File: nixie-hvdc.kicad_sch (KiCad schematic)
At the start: 13 parts, among them Q1 IRF740, U1 MAX1771xSA

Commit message: almost done
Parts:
- added D3: PTVS18VZ1USK, Diode_SMD:Nexperia_DSN1608-2_1.6x0.8mm, symbol Diode:PTVS18VZ1USK
- added F1: 2A, symbol Device:Fuse
- added FB1: FerriteBead, symbol Device:FerriteBead
- added J1: USB_C_Receptacle_PowerOnly_6P, Connector_USB:USB_C_Receptacle_HRO_TYPE-C-31-M-17, symbol Connector:USB_C_Receptacle_PowerOnly_6P
- added J2, J3: Screw_Terminal_01x02, TerminalBlock_Phoenix:TerminalBlock_Phoenix_MKDS-1,5-2-5.08_1x02_P5.08mm_Horizontal, symbol Connector:Screw_Terminal_01x02
- added J4: Conn_01x10_Socket, Connector_PinHeader_2.54mm:PinHeader_1x10_P2.54mm_Vertical, symbol Connector:Conn_01x10_Socket
- added NX1: IN-12A, nixies-us:nixies-us-IN-12-DSUB-NOHOLE, symbol nixies-us:IN-12A
- added Q10, Q11, Q2, Q3, Q4, Q5, Q6, Q7, Q8, Q9: MPSA42, Package_TO_SOT_THT:TO-92_Inline, symbol Transistor_BJT:MPSA42
- added R10, R11, R12, R13, R14, R15, R16, R6, R7, R8, R9: 10k, symbol Device:R_US
- added R4, R5: 5.1k, symbol Device:R_US
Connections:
- net 180V: now also J3.1 (Pin_1), R6.2
- net GND: now also D3.1 (K), J1.A12 (GND), J1.B12 (GND), J1.S1 (SHIELD), J2.1 (Pin_1), J3.2 (Pin_2), Q10.1 (E), Q11.1 (E), Q2.1 (E), Q3.1 (E), Q4.1 (E), Q5.1 (E), Q6.1 (E), Q7.1 (E), Q8.1 (E), Q9.1 (E), R4.2, R5.2
- net at L1.2, Q1.2 (D): now also D1.2 (A)
- net +3V3: no longer names the net of C2.1, C3.1, L1.1, U1.2 (V+)
- net +3V3: now also FB1.2; no longer D1.2 (A)
- new net: Q2.2 (B), R7.2
- new net: Q6.2 (B), R11.2
- new net: Q10.2 (B), R15.2
- new net: Q8.2 (B), R13.2
- new net: Q11.2 (B), R16.2
- new net: Q3.2 (B), R8.2
- new net: Q5.2 (B), R10.2
- new net: J1.B5 (CC2), R4.1
- new net: Q7.2 (B), R12.2
- new net: NX1.A, R6.1
- new net: J1.A5 (CC1), R5.1
- new net: Q9.2 (B), R14.2
- new net: D3.2 (A), F1.2, FB1.1
- new net: Q4.2 (B), R9.2
- new net +12V: F1.1, J2.2 (Pin_2)
- new net +5V: J1.A9 (VBUS), J1.B9 (VBUS)
- new net CTRL_DIGIT_0: J4.10 (Pin_10), R7.1
- new net CTRL_DIGIT_1: J4.1 (Pin_1), R8.1
- new net CTRL_DIGIT_2: J4.2 (Pin_2), R9.1
- new net CTRL_DIGIT_3: J4.3 (Pin_3), R13.1
- new net CTRL_DIGIT_4: J4.4 (Pin_4), R14.1
- new net CTRL_DIGIT_5: J4.5 (Pin_5), R15.1
- new net CTRL_DIGIT_6: J4.6 (Pin_6), R10.1
- new net CTRL_DIGIT_7: J4.7 (Pin_7), R11.1
- new net CTRL_DIGIT_8: J4.8 (Pin_8), R12.1
- new net CTRL_DIGIT_9: J4.9 (Pin_9), R16.1
- new net NIXIE_DIGIT_0: NX1.0, Q2.3 (C)
- new net NIXIE_DIGIT_1: NX1.1, Q3.3 (C)
- new net NIXIE_DIGIT_2: NX1.2, Q4.3 (C)
- new net NIXIE_DIGIT_3: NX1.3, Q8.3 (C)
- new net NIXIE_DIGIT_4: NX1.4, Q9.3 (C)
- new net NIXIE_DIGIT_5: NX1.5, Q10.3 (C)
- new net NIXIE_DIGIT_6: NX1.6, Q5.3 (C)
- new net NIXIE_DIGIT_7: NX1.7, Q6.3 (C)
- new net NIXIE_DIGIT_8: NX1.8, Q7.3 (C)
- new net NIXIE_DIGIT_9: NX1.9, Q11.3 (C)
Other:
- note added: "TODOs: - [ ] figure out how drive mosfet gate with just 5V input instead of 12V - [ ] verify current, voltage ratings of components - [ ] finalize BOM - [ ] check if my tube is hole/no-hole variant. for footprint"
- note removed: "TODOs: - add usb connector for V_in (5V) - add block terminal connectors for V_in - add block terminals for V_out (180V) - connect V_out, GND to nixie tube symbol - check output current of this circuit"
- moved on the sheet: C1, C2, C3, C4, C5, D1, L1, Q1, R1, R2, R3, RV1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

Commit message: schematic done, bom done
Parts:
- removed D3: PTVS18VZ1USK, Diode_SMD:Nexperia_DSN1608-2_1.6x0.8mm, symbol Diode:PTVS18VZ1USK
- removed F1: 2A, symbol Device:Fuse
- removed FB1: FerriteBead, symbol Device:FerriteBead
- removed J1: USB_C_Receptacle_PowerOnly_6P, Connector_USB:USB_C_Receptacle_HRO_TYPE-C-31-M-17, symbol Connector:USB_C_Receptacle_PowerOnly_6P
- removed R4, R5: 5.1k, symbol Device:R_US
- added J1: PJ-002B, barrel_jack:CUI_PJ-002B, symbol Connector:Barrel_Jack_Switch
- C1: renamed from C3; value 100uF/200V -> 100uF/20V; footprint (none) -> Capacitor_Tantalum_SMD:CP_EIA-7343-31_Kemet-D_HandSolder; DigiKey Part No. (none) -> 478-1724-2-ND; LCSC Part No. (none) -> C122302
- C2: value 0.1 uF -> 0.1uF/25V; footprint (none) -> Capacitor_SMD:C_0805_2012Metric_Pad1.18x1.45mm_HandSolder; DigiKey Part No. (none) -> 478-KGM21NR71E104KTTR-ND; LCSC Part No. (none) -> C396718
- C3: renamed from C1; value 0.1 uF -> 0.1uF/25V; footprint (none) -> Capacitor_SMD:C_0805_2012Metric_Pad1.18x1.45mm_HandSolder; DigiKey Part No. (none) -> 478-KGM21NR71E104KTTR-ND; LCSC Part No. (none) -> C396718
- C4: value 4.7uF/200V -> 4.7uF/250V; footprint (none) -> Capacitor_SMD:CP_Elec_8x10.5; DigiKey Part No. (none) -> 493-9983-2-ND; LCSC Part No. (none) -> C88702
- C5: footprint (none) -> Capacitor_SMD:C_1210_3225Metric_Pad1.33x2.70mm_HandSolder; DigiKey Part No. (none) -> 1292-1617-2-ND; LCSC Part No. (none) -> C52020
- D2: renamed from D1; footprint (none) -> Diode_SMD:D_SMB-SMC_Universal_Handsoldering; DigiKey Part No. (none) -> 1801-ES2FTR-ND; LCSC Part No. (none) -> C2844160; MFR Part No. (none) -> ES2GB
- J2: DigiKey Part No. (none) -> 277-1548128-ND; LCSC Part No. (none) -> C5183929; MFR Part No. (none) -> MKDS 1,5/ 2-5,08
- J3: renamed from J4; DigiKey Part No. (none) -> TS-112-T-A-1-ND; LCSC Part No. (none) -> C492409
- J4: renamed from J3; DigiKey Part No. (none) -> 277-1548128-ND; LCSC Part No. (none) -> C5183929; MFR Part No. (none) -> MKDS 1,5/ 2-5,08
- L1: footprint Inductor_SMD:L_0805_2012Metric_Pad1.15x1.40mm_HandSolder -> Inductor_SMD:L_12x12mm_H6mm; DigiKey Part No. (none) -> SRR1260-101MTR-ND; LCSC Part No. (none) -> C2962892; MFR Part No. PSPMAA0805-101M-ANP -> (none)
- NX1: footprint nixies-us:nixies-us-IN-12-DSUB-NOHOLE -> nixies-us:nixies-us-IN-12-DSUB
- Q1: renamed from Q2; footprint Package_TO_SOT_THT:TO-92_Inline -> Package_TO_SOT_THT:TO-92; DigiKey Part No. (none) -> MPSA42FS-ND; LCSC Part No. (none) -> C305411; MFR Part No. (none) -> MPSA42
- Q10: renamed from Q11; footprint Package_TO_SOT_THT:TO-92_Inline -> Package_TO_SOT_THT:TO-92; DigiKey Part No. (none) -> MPSA42FS-ND; LCSC Part No. (none) -> C305411; MFR Part No. (none) -> MPSA42
- Q11: renamed from Q1; DigiKey Part No. (none) -> IRF740PBF-ND; LCSC Part No. (none) -> C34373758; MFR Part No. (none) -> IRF740PBF
- Q2: renamed from Q10; footprint Package_TO_SOT_THT:TO-92_Inline -> Package_TO_SOT_THT:TO-92; DigiKey Part No. (none) -> MPSA42FS-ND; LCSC Part No. (none) -> C305411; MFR Part No. (none) -> MPSA42
- Q3, Q6, Q9: footprint Package_TO_SOT_THT:TO-92_Inline -> Package_TO_SOT_THT:TO-92; DigiKey Part No. (none) -> MPSA42FS-ND; LCSC Part No. (none) -> C305411; MFR Part No. (none) -> MPSA42
- Q4: renamed from Q5; footprint Package_TO_SOT_THT:TO-92_Inline -> Package_TO_SOT_THT:TO-92; DigiKey Part No. (none) -> MPSA42FS-ND; LCSC Part No. (none) -> C305411; MFR Part No. (none) -> MPSA42
- Q5: renamed from Q4; footprint Package_TO_SOT_THT:TO-92_Inline -> Package_TO_SOT_THT:TO-92; DigiKey Part No. (none) -> MPSA42FS-ND; LCSC Part No. (none) -> C305411; MFR Part No. (none) -> MPSA42
- Q7: renamed from Q8; footprint Package_TO_SOT_THT:TO-92_Inline -> Package_TO_SOT_THT:TO-92; DigiKey Part No. (none) -> MPSA42FS-ND; LCSC Part No. (none) -> C305411; MFR Part No. (none) -> MPSA42
- Q8: renamed from Q7; footprint Package_TO_SOT_THT:TO-92_Inline -> Package_TO_SOT_THT:TO-92; DigiKey Part No. (none) -> MPSA42FS-ND; LCSC Part No. (none) -> C305411; MFR Part No. (none) -> MPSA42
- R1: renamed from R7; footprint (none) -> Resistor_SMD:R_0805_2012Metric_Pad1.20x1.40mm_HandSolder; DigiKey Part No. (none) -> 2019-RK73H2ATTD1002FTR-ND; LCSC Part No. (none) -> C269724
- R10: renamed from R16; footprint (none) -> Resistor_SMD:R_0805_2012Metric_Pad1.20x1.40mm_HandSolder; DigiKey Part No. (none) -> 2019-RK73H2ATTD1002FTR-ND; LCSC Part No. (none) -> C269724
- R11: renamed from R1; footprint (none) -> Resistor_SMD:R_1206_3216Metric_Pad1.30x1.75mm_HandSolder; DigiKey Part No. (none) -> HCS1206FTL500TR-ND; LCSC Part No. (none) -> C149662
- R12: renamed from R2; footprint (none) -> Resistor_SMD:R_0805_2012Metric_Pad1.20x1.40mm_HandSolder; DigiKey Part No. (none) -> RHM1.5MKTR-ND; LCSC Part No. (none) -> 125mW Thick Film Resistor ±200ppm/℃ ±1% 1.5MΩ 0805 Chip Res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
- R13: renamed from R3; value 10K -> 10k; footprint (none) -> Resistor_SMD:R_0805_2012Metric_Pad1.20x1.40mm_HandSolder; DigiKey Part No. (none) -> 2019-RK73H2ATTD1002FTR-ND; LCSC Part No. (none) -> C269724
- R14: renamed from R6; footprint (none) -> Resistor_SMD:R_0805_2012Metric_Pad1.20x1.40mm_HandSolder; DigiKey Part No. (none) -> 2019-RK73H2ATTD1002FTR-ND; LCSC Part No. (none) -> C269724
- R2: renamed from R15; footprint (none) -> Resistor_SMD:R_0805_2012Metric_Pad1.20x1.40mm_HandSolder; DigiKey Part No. (none) -> 2019-RK73H2ATTD1002FTR-ND; LCSC Part No. (none) -> C269724
- R3: renamed from R8; footprint (none) -> Resistor_SMD:R_0805_2012Metric_Pad1.20x1.40mm_HandSolder; DigiKey Part No. (none) -> 2019-RK73H2ATTD1002FTR-ND; LCSC Part No. (none) -> C269724
- R4: renamed from R10; footprint (none) -> Resistor_SMD:R_0805_2012Metric_Pad1.20x1.40mm_HandSolder; DigiKey Part No. (none) -> 2019-RK73H2ATTD1002FTR-ND; LCSC Part No. (none) -> C269724
- R5: renamed from R9; footprint (none) -> Resistor_SMD:R_0805_2012Metric_Pad1.20x1.40mm_HandSolder; DigiKey Part No. (none) -> 2019-RK73H2ATTD1002FTR-ND; LCSC Part No. (none) -> C269724
- R6: renamed from R11; footprint (none) -> Resistor_SMD:R_0805_2012Metric_Pad1.20x1.40mm_HandSolder; DigiKey Part No. (none) -> 2019-RK73H2ATTD1002FTR-ND; LCSC Part No. (none) -> C269724
- R7: renamed from R13; footprint (none) -> Resistor_SMD:R_0805_2012Metric_Pad1.20x1.40mm_HandSolder; DigiKey Part No. (none) -> 2019-RK73H2ATTD1002FTR-ND; LCSC Part No. (none) -> C269724
- R8: renamed from R12; footprint (none) -> Resistor_SMD:R_0805_2012Metric_Pad1.20x1.40mm_HandSolder; DigiKey Part No. (none) -> 2019-RK73H2ATTD1002FTR-ND; LCSC Part No. (none) -> C269724
- R9: renamed from R14; footprint (none) -> Resistor_SMD:R_0805_2012Metric_Pad1.20x1.40mm_HandSolder; DigiKey Part No. (none) -> 2019-RK73H2ATTD1002FTR-ND; LCSC Part No. (none) -> C269724
- RV1: value VG039NCHXTB502 -> VGF39NCHXT-B502; footprint (none) -> Potentiometer_SMD:Potentiometer_Bourns_TC33X_Vertical; DigiKey Part No. (none) -> TC33X-502ETR-ND; LCSC Part No. (none) -> C22461636; MFR Part No. (none) -> VGF39NCHXT-B502
- U1: DigiKey Part No. (none) -> MAX1771CSA+TR-ND; LCSC Part No. (none) -> C407903; MFR Part No. (none) -> MAX1771
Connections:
- net +12V: now also C1.1, C2.1, L1.1, U1.2 (V+), J1.1
- net GND: now also J1.2
- no-connect marks 0 -> 1
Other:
- note removed: "TODOs: - [ ] figure out how drive mosfet gate with just 5V input instead of 12V - [ ] verify current, voltage ratings of components - [ ] finalize BOM - [ ] check if my tube is hole/no-hole variant. for footprint"
- moved on the sheet: J2, J3, NX1, R14

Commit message: starting pcb layout
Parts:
- C1: DigiKey Part No. 478-1724-2-ND -> 478-6066-2-ND
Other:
- note added: "Ref: - https://www.electronics-lab.com/project/hv-nixie-dc-dc-switching-power-supply/ - https://nick.desmith.net/Electronics/NixiePSU.html"
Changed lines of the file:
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@@
 		(company "yashkarthik.com")
 	)
+	(text "Ref: \n- https://www.electronics-lab.com/project/hv-nixie-dc-dc-switching-power-supply/\n- https://nick.desmith.net/Electronics/NixiePSU.html\n"
+		(exclude_from_sim no)
+		(at 176.276 161.29 0)
+		(effects
+			(font
+				(size 1.27 1.27)
+			)
+			(justify left)
+		)
+	)
 	(junction
 		(at 210.82 41.91)
@@
 			)
 		)
-		(property "DigiKey Part No." "478-1724-2-ND"
+		(property "DigiKey Part No." "478-6066-2-ND"
 			(at 121.92 40.64 0)
 			(effects

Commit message: more
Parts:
- removed C4: 4.7uF/250V, Capacitor_SMD:CP_Elec_8x10.5, symbol Device:C
- removed J3: Conn_01x10_Socket, Connector_PinHeader_2.54mm:PinHeader_1x10_P2.54mm_Vertical, symbol Connector:Conn_01x10_Socket
- removed NX1: IN-12A, nixies-us:nixies-us-IN-12-DSUB, symbol nixies-us:IN-12A
- added C4: 4.7uF/250V, Capacitor_SMD:CP_Elec_8x10.5, symbol Device:C_US
- added J1: Conn_01x11_Pin, Connector_PinHeader_2.54mm:PinHeader_1x11_P2.54mm_Vertical, symbol Connector:Conn_01x11_Pin
- added NX1: IN-12BIN-12-DSUB, nixies-us:nixies-us-IN-12-DSUB, symbol nixies-us:IN-12BIN-12-DSUB
- added Q11: MPSA42, Package_TO_SOT_THT:TO-92, symbol Transistor_BJT:MPSA42
- added R11: 2.2k, Resistor_SMD:R_0805_2012Metric_Pad1.20x1.40mm_HandSolder, symbol Device:R_US
- R1, R10, R2, R3, R4, R5, R6, R7, R8, R9: value 10k -> 2.2k; DigiKey Part No. 2019-RK73H2ATTD1002FTR-ND -> A106060TR-ND
- R14: value 10k -> 22k; DigiKey Part No. 2019-RK73H2ATTD1002FTR-ND -> A129765TR-ND
- renumbered D2 to D1, J1 to J2, J2 to J3, Q11 to Q12, R11 to R_SENSE1
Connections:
- net 180V: now also C4.1
- net CTRL_DIGIT_0: now also J1.2 (Pin_2)
- net CTRL_DIGIT_1: now also J1.11 (Pin_11)
- net CTRL_DIGIT_2: now also J1.10 (Pin_10)
- net CTRL_DIGIT_3: now also J1.9 (Pin_9)
- net CTRL_DIGIT_4: now also J1.8 (Pin_8)
- net CTRL_DIGIT_5: now also J1.7 (Pin_7)
- net CTRL_DIGIT_6: now also J1.6 (Pin_6)
- net CTRL_DIGIT_7: now also J1.5 (Pin_5)
- net CTRL_DIGIT_8: now also J1.4 (Pin_4)
- net CTRL_DIGIT_9: now also J1.3 (Pin_3)
- net GND: now also C4.2, Q11.1 (E)
- net NIXIE_DIGIT_0: now also NX1.0
- net NIXIE_DIGIT_1: now also NX1.1
- net NIXIE_DIGIT_2: now also NX1.2
- net NIXIE_DIGIT_3: now also NX1.3
- net NIXIE_DIGIT_4: now also NX1.4
- net NIXIE_DIGIT_5: now also NX1.5
- net NIXIE_DIGIT_6: now also NX1.6
- net NIXIE_DIGIT_7: now also NX1.7
- net NIXIE_DIGIT_8: now also NX1.8
- net NIXIE_DIGIT_9: now also NX1.9
- net at R14.1: now also NX1.A
- new net: Q11.2 (B), R11.2
- new net CTRL_DIGIT_LHDP: J1.1 (Pin_1), R11.1
- new net NIXIE_DIGIT_LHDP: NX1.LHDP, Q11.3 (C)
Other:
- moved on the sheet: R14

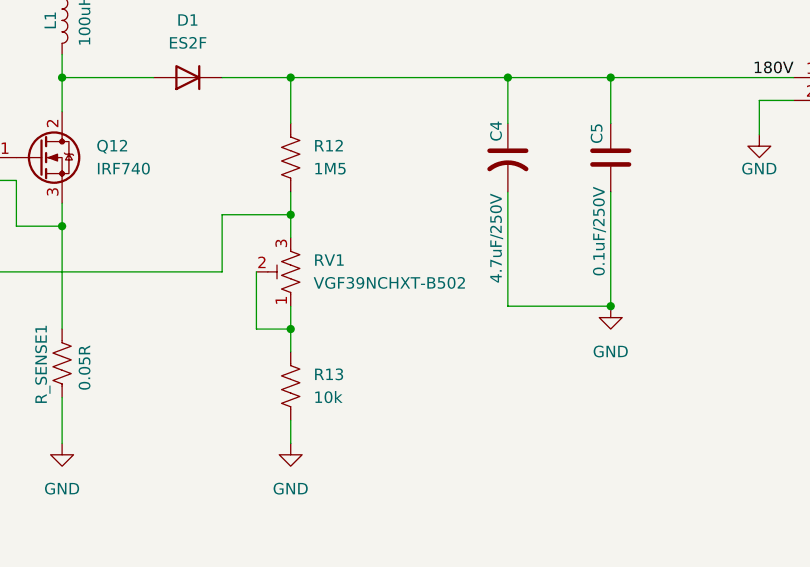
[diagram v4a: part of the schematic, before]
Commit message: change pot
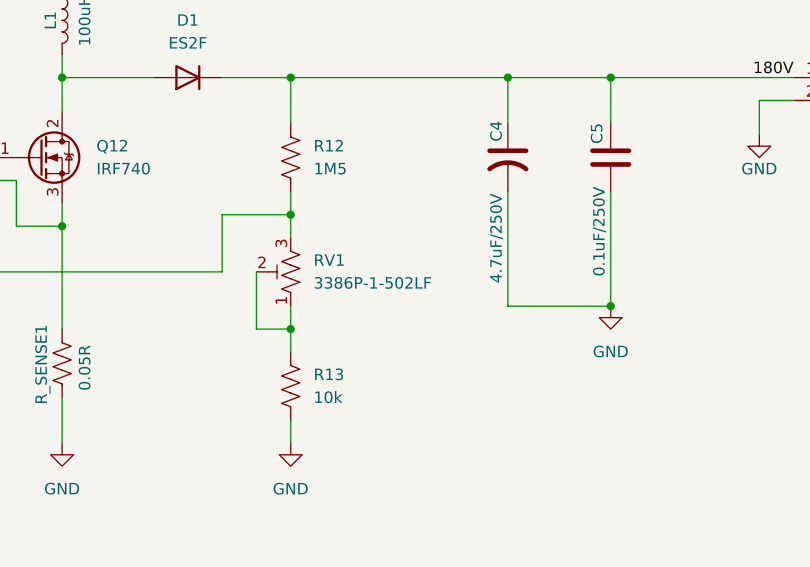
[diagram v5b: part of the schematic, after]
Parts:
- RV1: value VGF39NCHXT-B502 -> 3386P-1-502LF; footprint Potentiometer_SMD:Potentiometer_Bourns_TC33X_Vertical -> Potentiometer_THT:Potentiometer_Bourns_3386P_Vertical; DigiKey Part No. TC33X-502ETR-ND -> 3386P-502LF-ND; MFR Part No. VGF39NCHXT-B502 -> 3386P-1-502LF
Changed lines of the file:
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@@
 			)
 		)
-		(property "Value" "VGF39NCHXT-B502"
+		(property "Value" "3386P-1-502LF"
 			(at 213.36 64.7699 0)
 			(effects
@@
 			)
 		)
-		(property "Footprint" "Potentiometer_SMD:Potentiometer_Bourns_TC33X_Vertical"
+		(property "Footprint" "Potentiometer_THT:Potentiometer_Bourns_3386P_Vertical"
 			(at 210.82 63.5 0)
 			(effects
@@
 			)
 		)
-		(property "MFR Part No." "VGF39NCHXT-B502"
+		(property "MFR Part No." "3386P-1-502LF"
 			(at 210.82 63.5 0)
 			(effects
@@
 			)
 		)
-		(property "DigiKey Part No." "TC33X-502ETR-ND"
+		(property "DigiKey Part No." "3386P-502LF-ND"
 			(at 210.82 63.5 0)
 			(effects

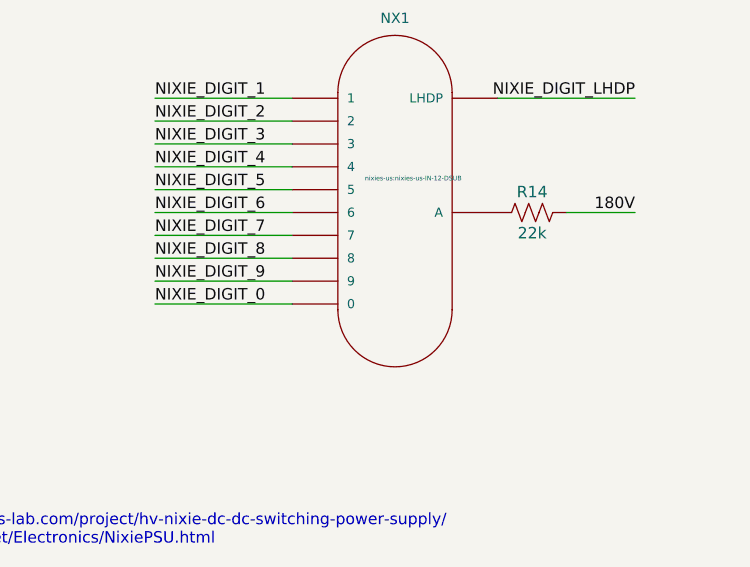
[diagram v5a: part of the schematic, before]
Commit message: fet orienatiton, r_sense vias
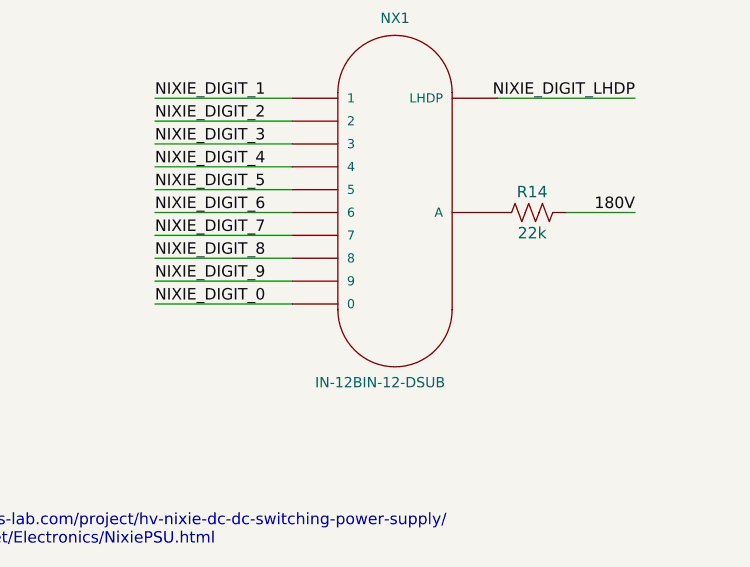
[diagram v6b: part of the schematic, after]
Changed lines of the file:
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@@
 		(on_board yes)
 		(dnp no)
-		(fields_autoplaced yes)
 		(property "Reference" "NX1"
 			(at 241.3 105.41 0)
@@
 		)
 		(property "Value" "IN-12BIN-12-DSUB"
-			(at 242.57 127 0)
+			(at 232.41 146.558 0)
 			(effects
 				(font
@@
 				)
 				(justify left bottom)
-				(hide yes)
 			)
 		)
@@
 					(size 0.508 0.508)
 				)
+				(hide yes)
 			)
 		)
